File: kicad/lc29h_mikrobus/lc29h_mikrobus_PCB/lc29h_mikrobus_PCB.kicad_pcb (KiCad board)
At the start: 2 copper layers, 27.4 x 58.7 mm, 46 parts, among them IC1 MIKROE-924, IC2 DS28E36BQ+U, IC3 74LVC1G3157GV,125, J1 Conn_Coaxial, J2 Conn_01x03_Pin, Q1 MMBT2222A, Q2 DMP3013SFV, Q4 BSS123L, Q5 BSS123L, Q6 MMBT2222A, SW1 SW_Nidec_CAS-120A1, U1 TXS0102DCU, U2 LC29H

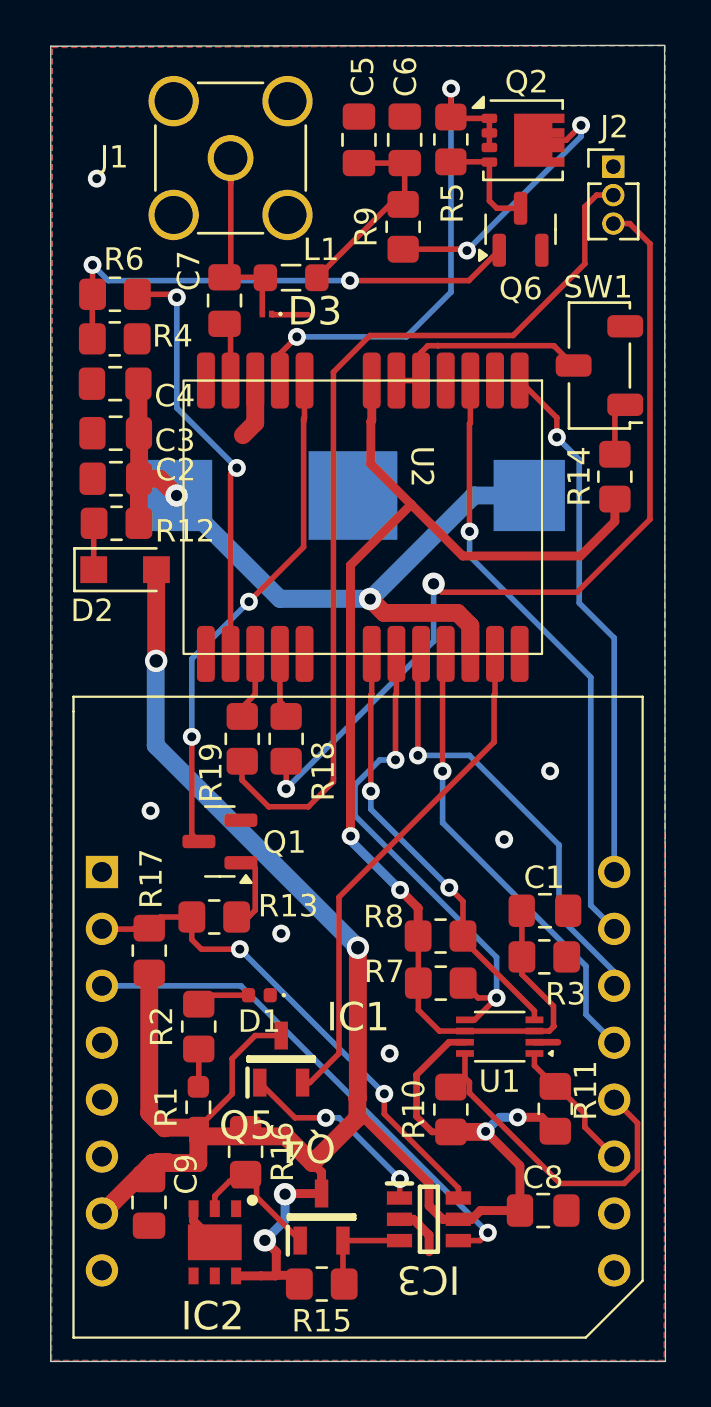
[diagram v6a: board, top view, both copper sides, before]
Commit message: pull up resistors and remove silkscreen warnings
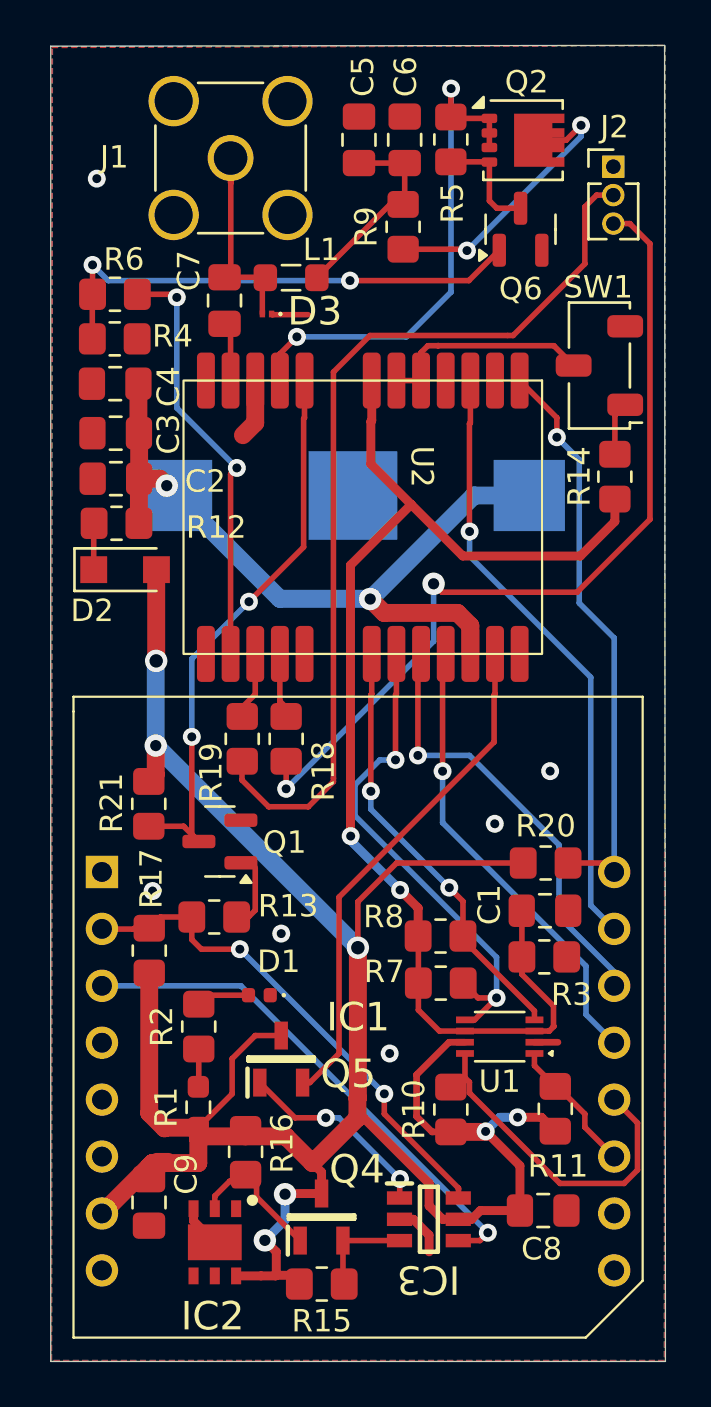
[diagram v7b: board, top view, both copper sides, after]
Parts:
- added R20: 10k, Resistor_SMD:R_0805_2012Metric_Pad1.20x1.40mm_HandSolder, F.Cu at (145.9, 74.8)
- added R21: 1.5k, Resistor_SMD:R_0805_2012Metric_Pad1.20x1.40mm_HandSolder, F.Cu at (128.2, 72.2)
- R13: value 2.2k -> 10k
- R18, R19: value 1k -> 10k
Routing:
- net VCC: track 97.8 -> 109.7 mm, vias 6 -> 7
- net Net-(Q1-C): track 23.0 -> 25.4 mm
- net WUP: track 23.7 -> 25.9 mm
